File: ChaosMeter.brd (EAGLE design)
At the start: 87.5 x 193.6 mm, 51 parts

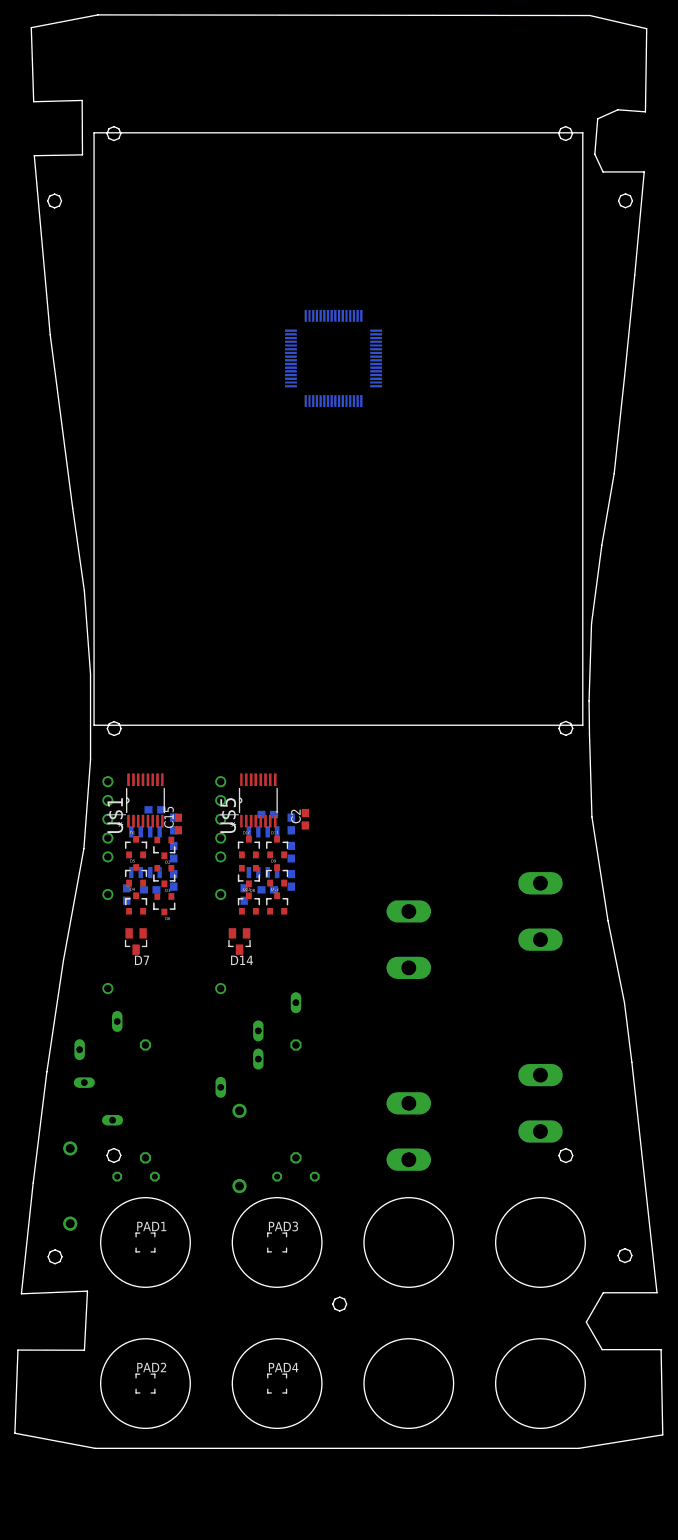
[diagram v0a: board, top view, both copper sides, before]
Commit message: Added double fuses (11A/440mA) for the amps input
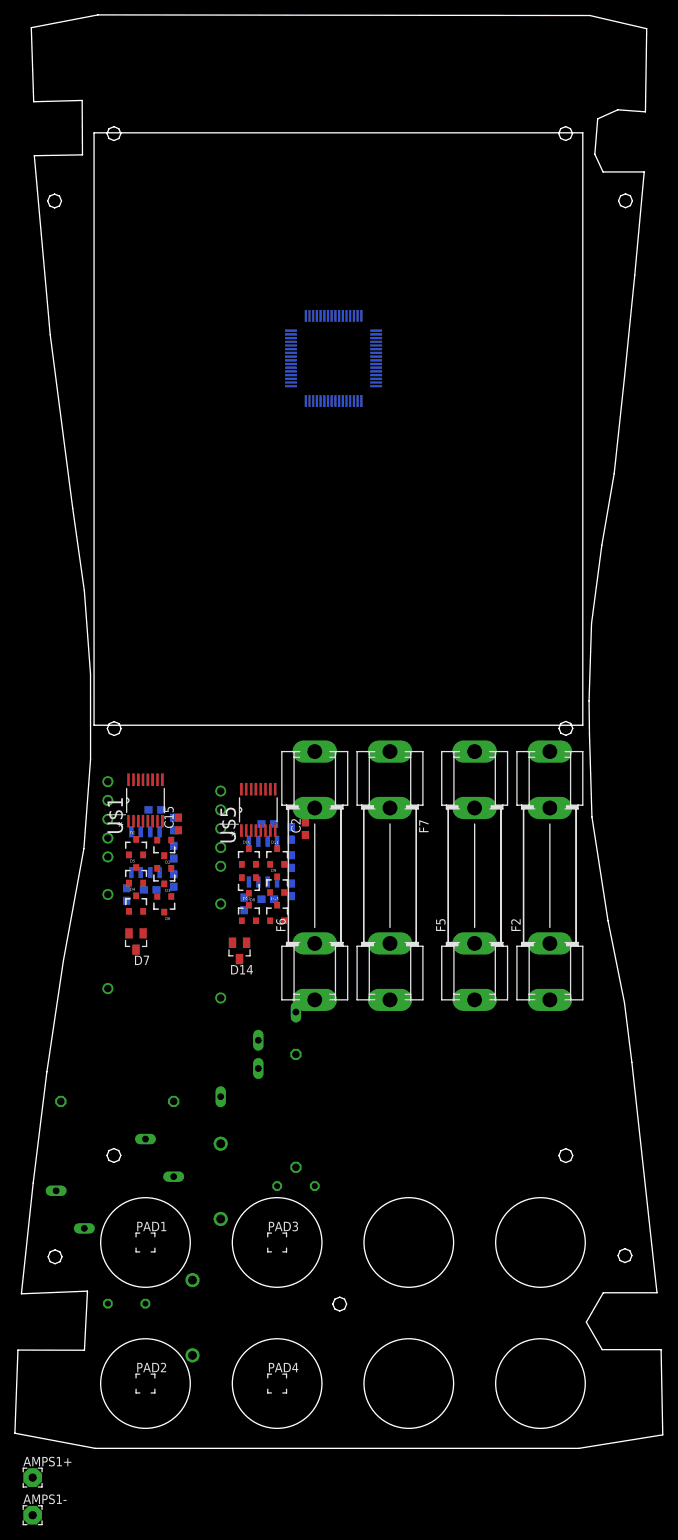
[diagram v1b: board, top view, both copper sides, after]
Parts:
- removed F1: FUSESH32, fuse:SH32
- added AMPS1+, AMPS1-: (no value), wirepad:2,54/1,1
- added F5, F7: 11A, fuse:SH32
- added F6: 440mA, fuse:SH32
- F2: value FUSESH32 -> 440mA
- moved F3 24.3 mm to (24.1, 17.8), turned to 90 degrees
- moved R8 18.5 mm to (19.7, 39.4), turned to 180 degrees
- moved F2 17.8 mm to (72.4, 77.5), flipped to the top, turned to 90 degrees
- moved R6 17.2 mm to (15.2, 19.7), turned to 0 degrees
- moved R7 15.1 mm to (7.62, 32.4), turned to 0 degrees
- moved F4 5.12 mm to (27.9, 36.2), turned to 90 degrees
- moved R5 3.81 mm to (14.0, 47.0), turned to 0 degrees
- moved C2 1.27 mm to (39.4, 83.8)
- moved C3 1.27 mm to (31.1, 73.7)
- moved R12 1.27 mm to (35.6, 57.1)
- moved R9 1.27 mm to (38.1, 45.7)
- moved U$4 1.27 mm to (27.9, 59.7)
- moved C10 1.27 mm to (34.3, 74.3)
- moved C11 1.27 mm to (34.3, 84.5)
- moved C6 1.27 mm to (37.5, 79.4)
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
